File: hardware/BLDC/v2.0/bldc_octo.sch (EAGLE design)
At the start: 5 parts, among them J1 PWR_2_XT30PW-M, J2 LINEAR_3_MOLEX_5023520300, J3 LINEAR_3_AMASS_MR30PW-M, U1 MA702, U2 STM32H723VGT6

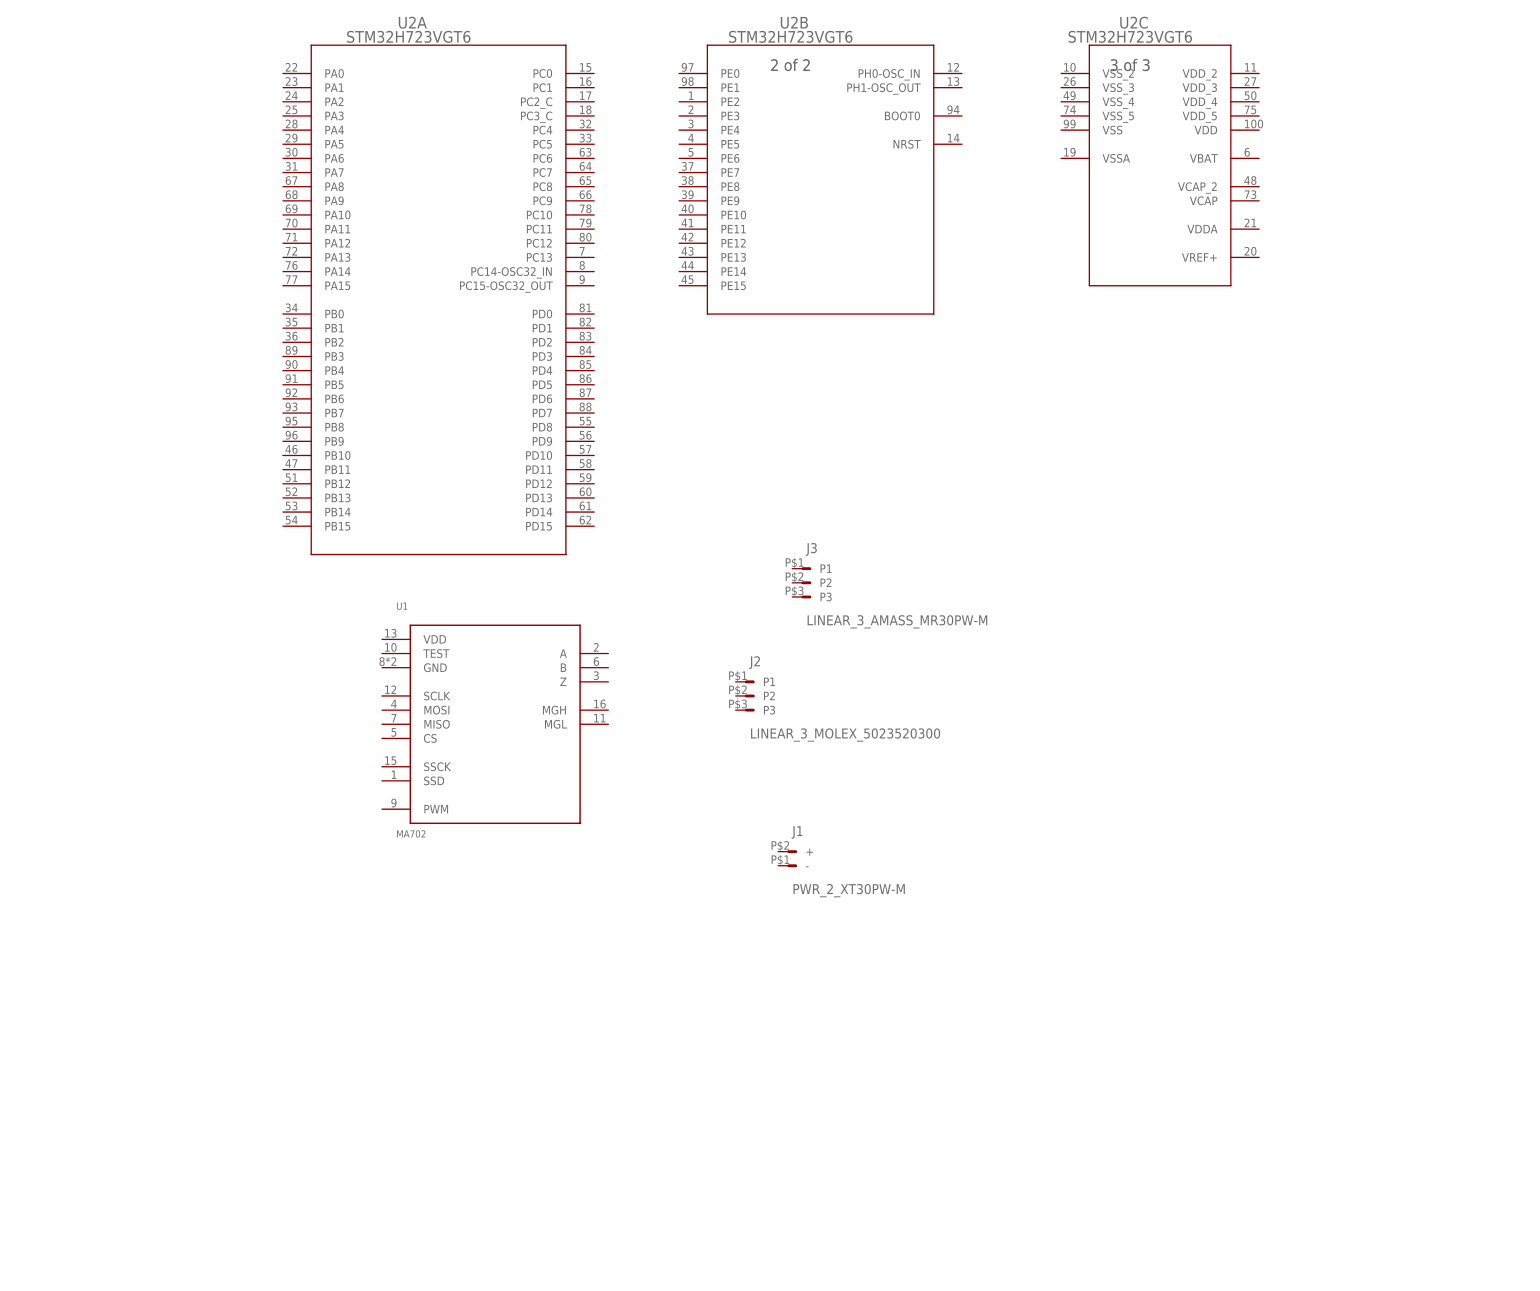
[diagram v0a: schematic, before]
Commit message: Added drv and 24MHz crystal
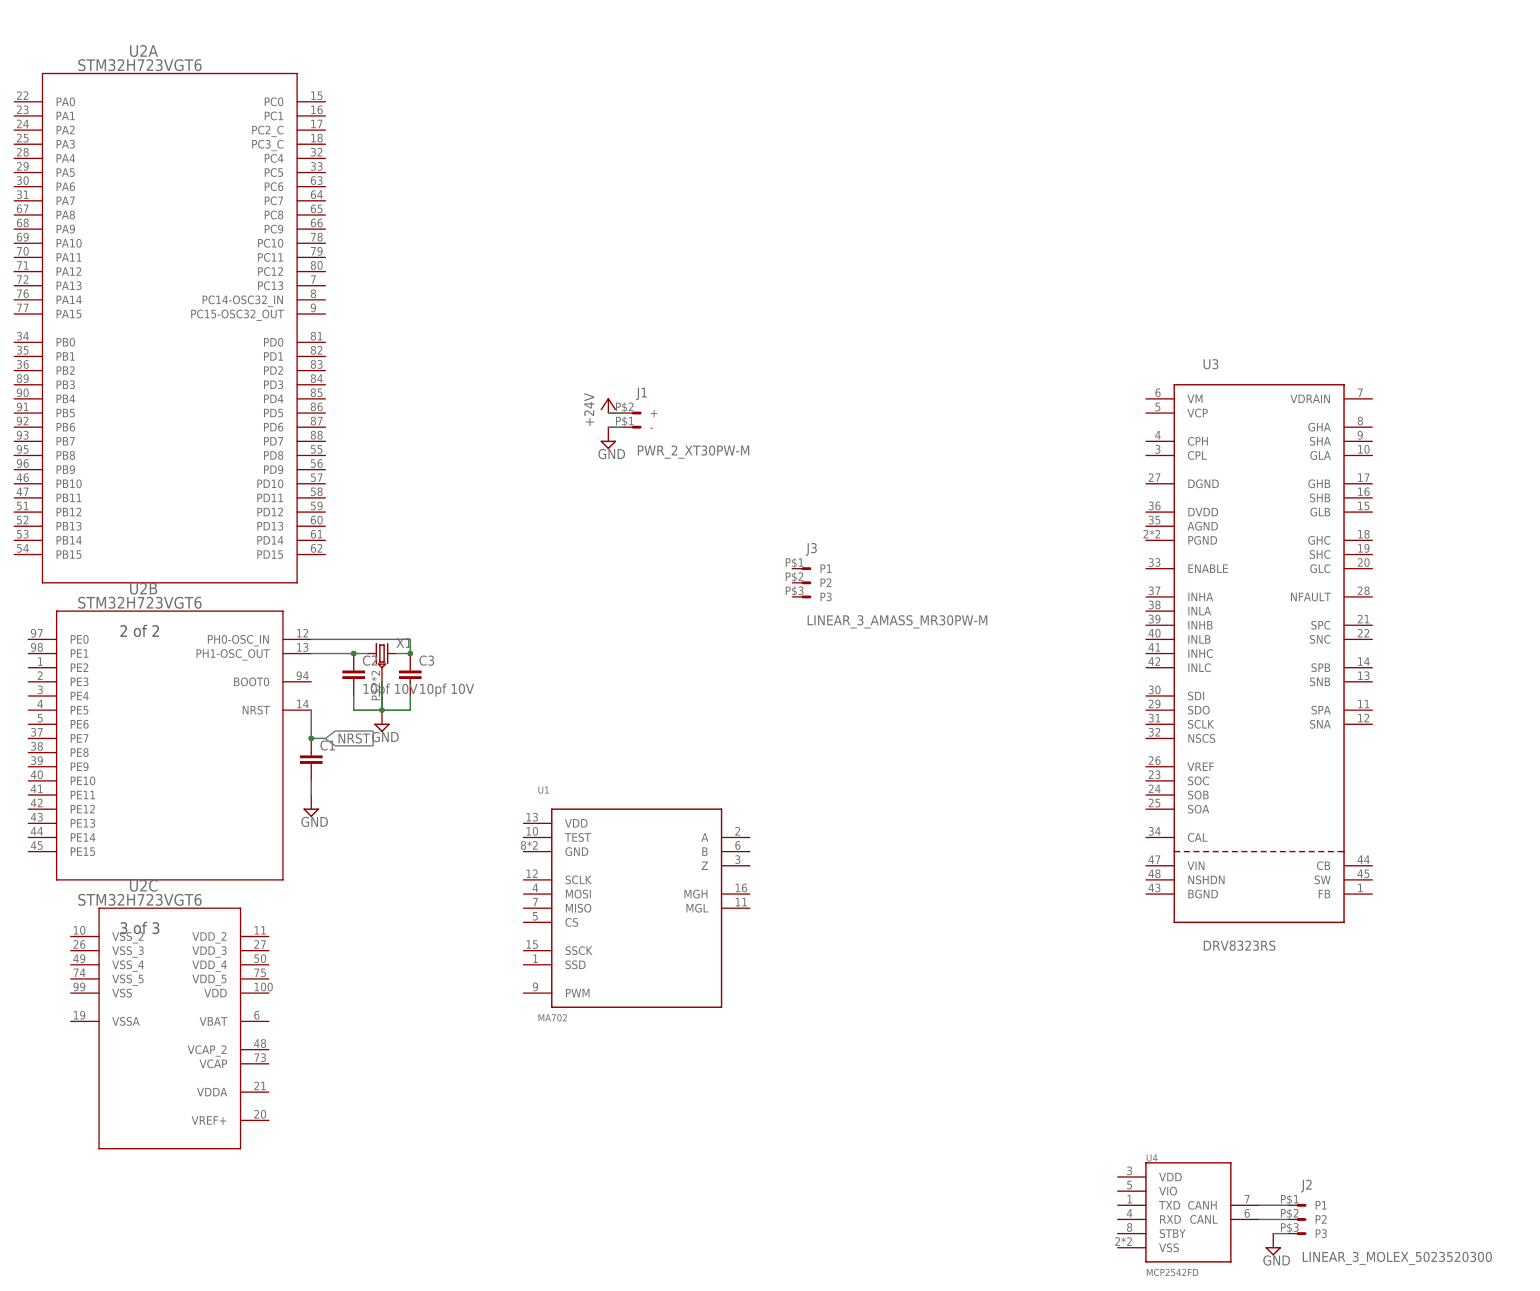
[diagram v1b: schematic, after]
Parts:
- added C1: (no value), _T_rcl:C0603
- added C2, C3: 10pf 10V, _T_rcl:C0603
- added U3: DRV8323RS, _T_ic:DRV8323RS
- added U4: MCP2542FD, _T_ic:MCP2542FD
- added X1: CRYSTAL_NX2016SA-24MHZ-EXS00A-CS11335, _T_ic:CRYSTAL_NX2016SA-24MHZ-EXS00A-CS11335
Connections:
- new net +24V: J1.+
- new net GND: C1.2, C2.2, C3.2, J1.-, J2.P3, X1.GND
- new net N$1: J2.P1, U4.CANH
- new net N$2: J2.P2, U4.CANL
- new net N$3: C2.1, U2B.PH1-OSC_OUT, X1.1
- new net N$4: C3.1, U2B.PH0-OSC_IN, X1.2
- new net NRST: C1.1, U2B.NRST
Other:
- moved on the sheet: J1, J2, U1, U2A, U2B, U2C
